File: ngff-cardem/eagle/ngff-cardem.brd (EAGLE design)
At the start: 90 x 100 mm, 146 parts, among them IC1 FPF2109, IC2 FPF2109, IC201 CB3Q3244PW, IC202 CB3Q3244PW, IC203 IP4234CZ6, IC302 TPS22958-DGN, J301 PJ-002BH-SMT-TR, M2 MENTOR_12701001, M3 MENTOR_12701001, Q201 12MHz, T1 BC847, T101 BC847, U201 IP4234CZ6, U202 AT91SAM3S-AU, U301 MIC5366-1.8YC5, X1 PINHD-2X3-SP, X102 ZX360D-B-10P(30), X201 MINI-USB-SHIELD-UX60-MB-5ST, X202 2.54mm, X3 JACK2.5_SJ-2523

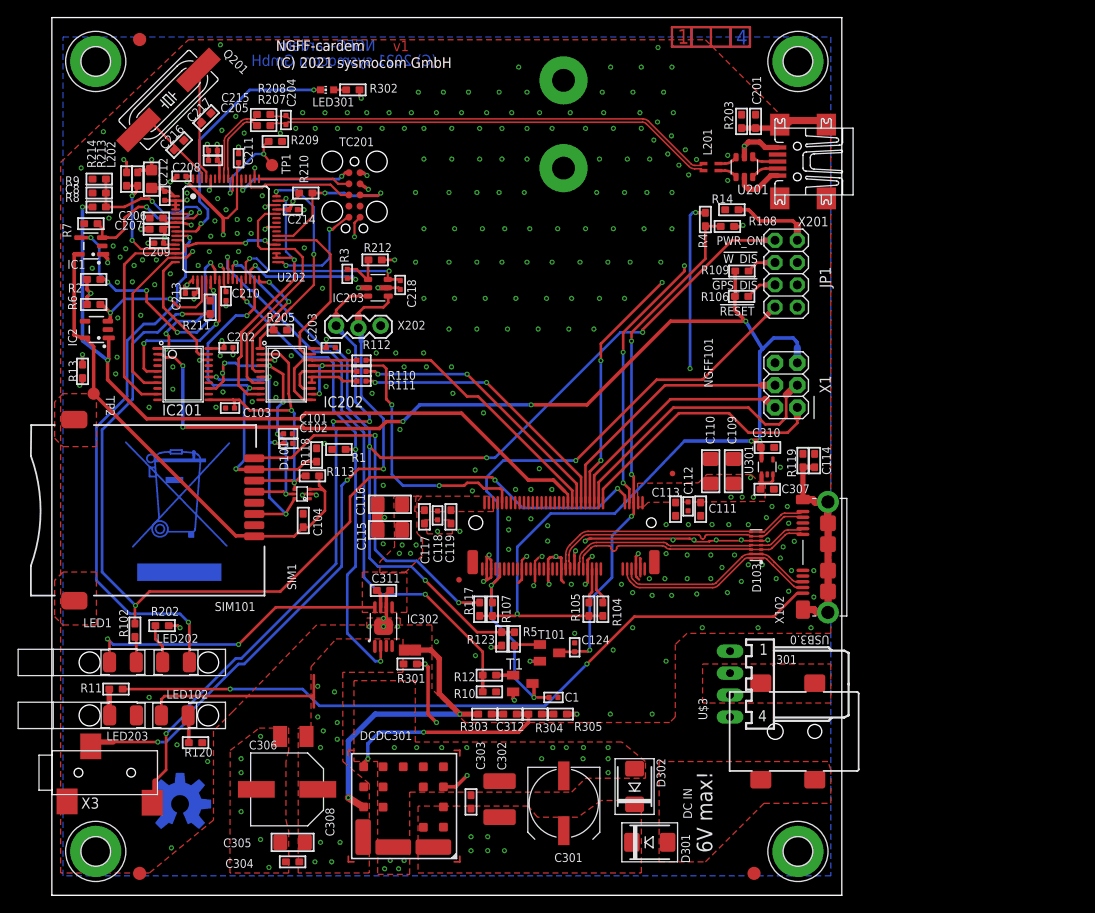
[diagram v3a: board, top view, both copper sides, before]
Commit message: ngff-cardem: add proper floppy power conn w/ a 2-resistor solder switch
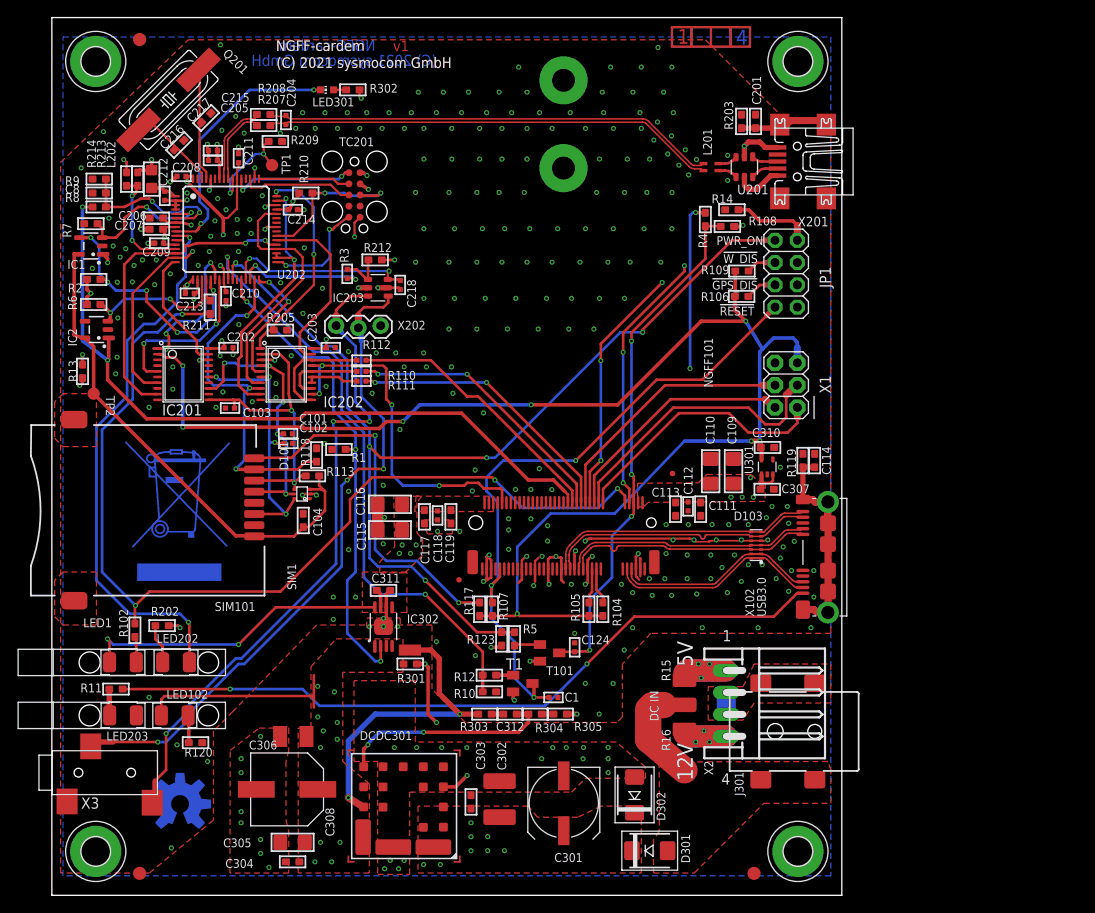
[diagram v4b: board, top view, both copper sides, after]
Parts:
- removed U$3: 171826-4-RA, 171826-4:171826-4
- added R15, R16: 0R, rc-sysmocom:1210
- added X2: 171826-4-RA, 171826-4:171826-4
- C311: value 100n -> 1n
- moved D301 0.95 mm to (68.1, 5.08)
- moved D302 0.95 mm to (66.4, 11.4)
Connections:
- new net N$23: R16.1, X2.4
- new net N$24: R15.2, X2.1
- net +VIN: now also R15.1, R16.2; no longer U$3.4
- net GND: now also X2.2, X2.3; no longer U$3.2, U$3.3
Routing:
- net N$24: track 0.00 -> 13.4 mm, vias 0 -> 3
- net +VIN: track 0.00 -> 13.3 mm
- net N$23: track 0.00 -> 12.8 mm, vias 0 -> 3
- net GND: track 98.3 -> 100.8 mm, vias 303 -> 312
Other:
- board text added: "12V"
- board text added: "5V"
- board text removed: "6V max!"

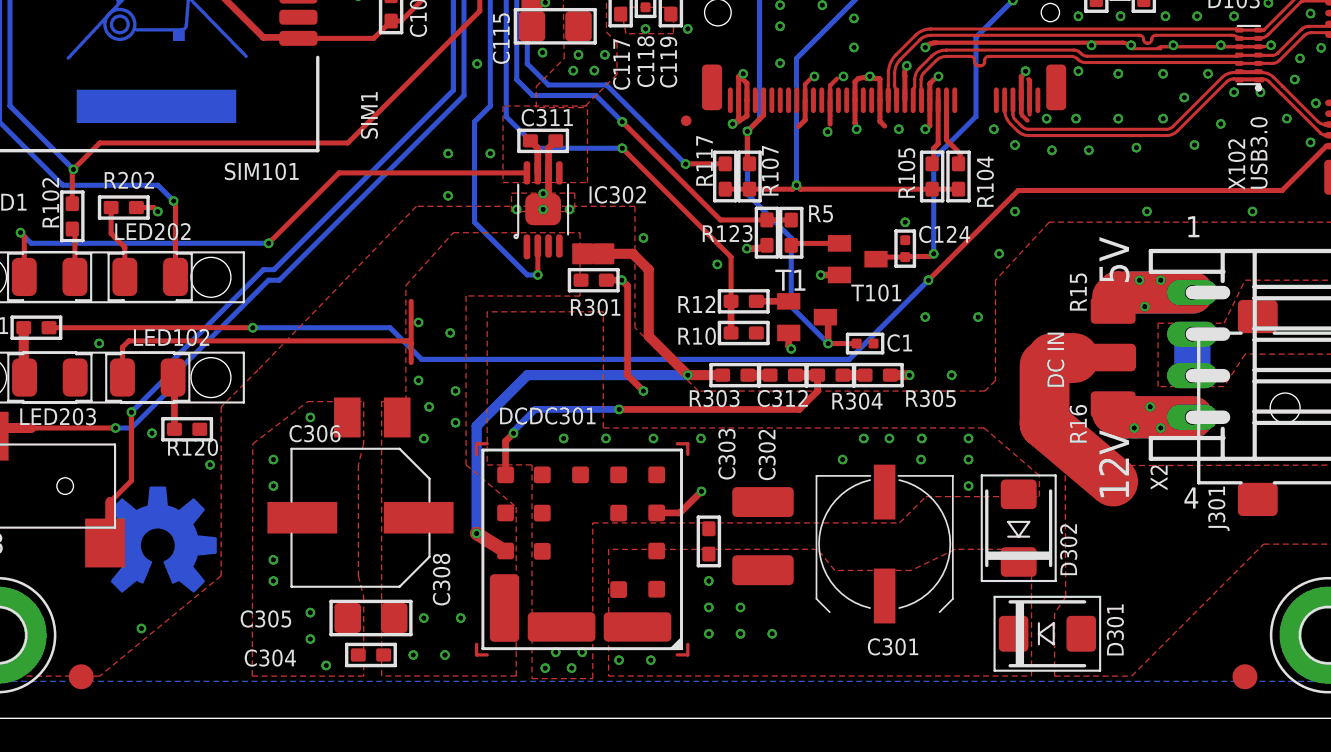
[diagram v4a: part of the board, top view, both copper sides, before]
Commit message: ngff-cardem: added a 2nd TPS22958 in VSSOP in parall due to availability
Now all four variant could be placed.
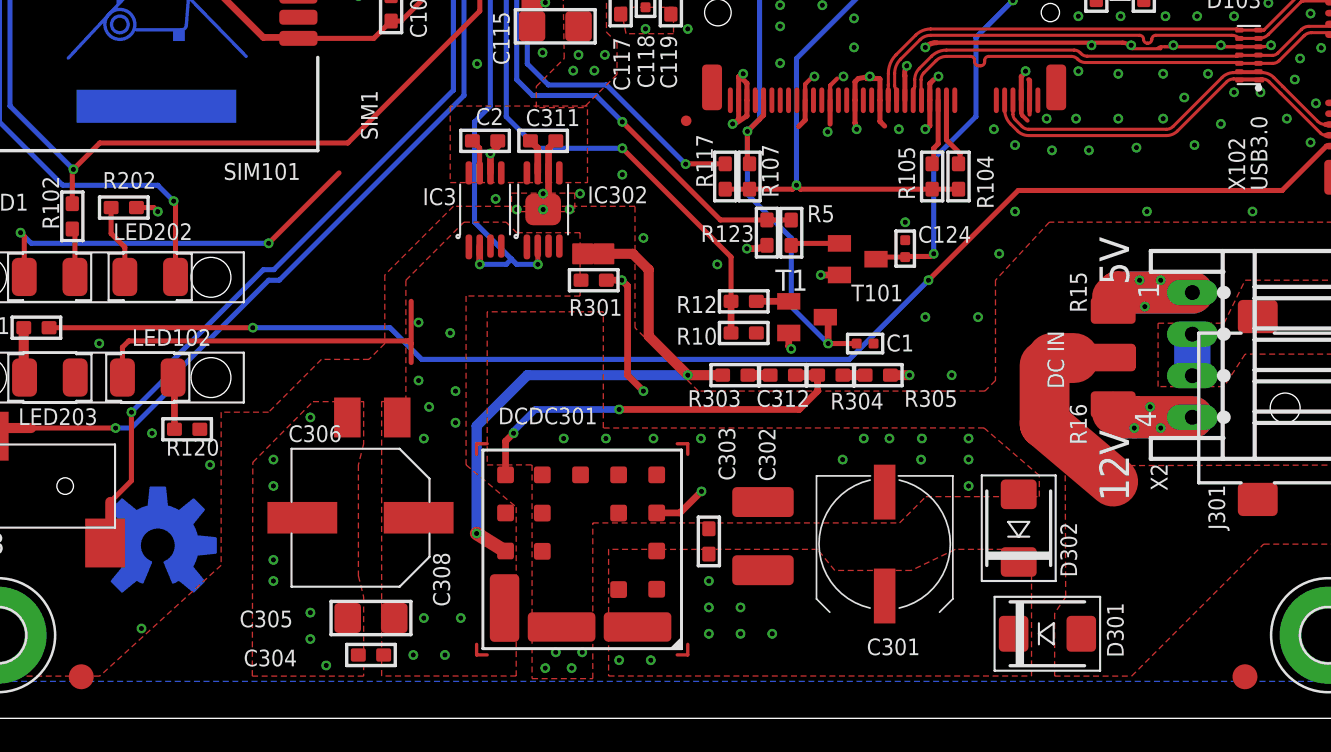
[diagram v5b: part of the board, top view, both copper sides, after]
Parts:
- added C2: 1n, rc-sysmocom:_0603
- added IC3: TPS22958N-DGK, TPS22958:VSSOP8
- IC302: value TPS22958-DGN -> TPS22958N-DGN; device TPS22958:VSSOP8-POWERPAD -> TPS22958:HVSSOP8
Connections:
- new net N$20: C2.2, IC3.7
- net GND: now also C2.1, IC3.6
- net MODEM_EN: now also IC3.2
- net VCC_3V3: now also IC3.1, IC3.3, IC3.4
- net V_MODEM: now also IC3.5, IC3.8
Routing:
- net V_MODEM: track 119.9 -> 108.6 mm
- net MODEM_EN: track 55.8 -> 58.0 mm, vias 3 -> 4
- net GND: track 100.8 -> 102.9 mm, vias 312 -> 313
- net N$20: track 0.00 -> 2.11 mm

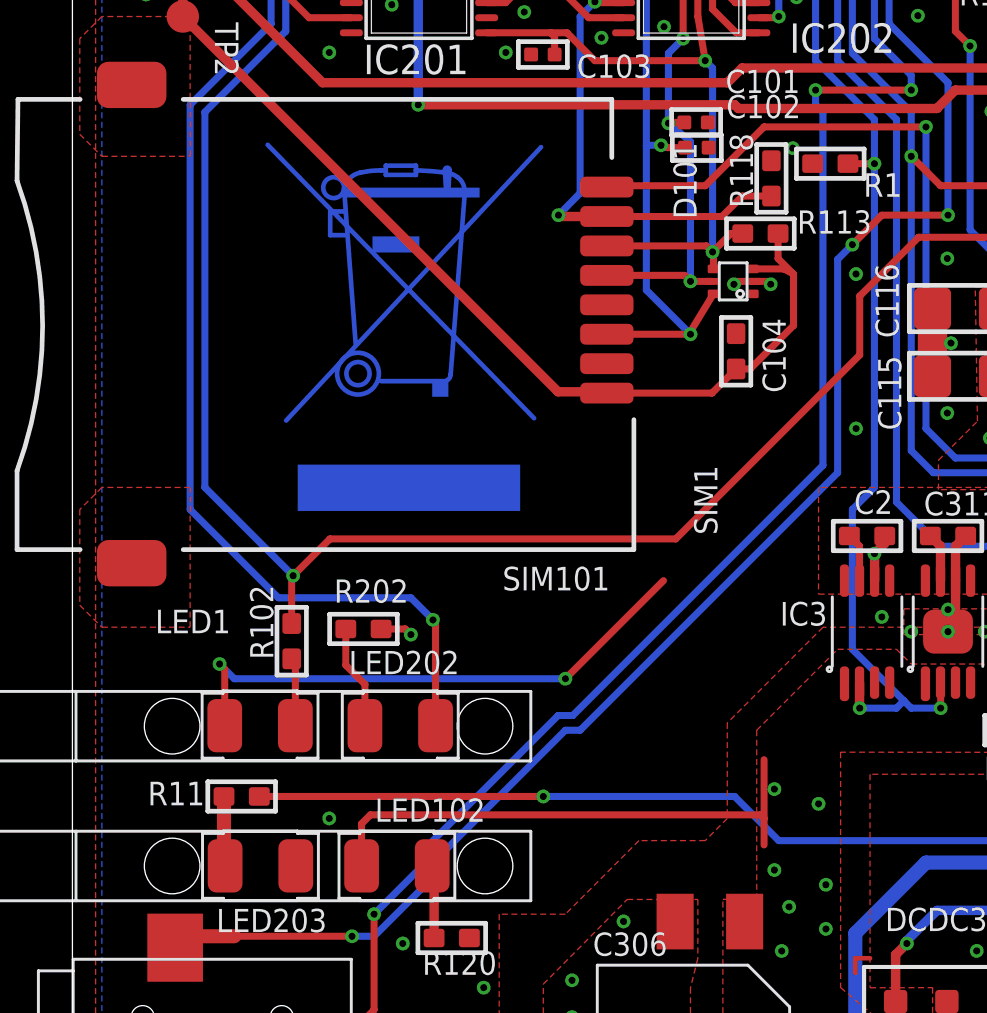
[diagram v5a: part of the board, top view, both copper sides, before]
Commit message: ngff-cardem: examine ERC + DRC for new part
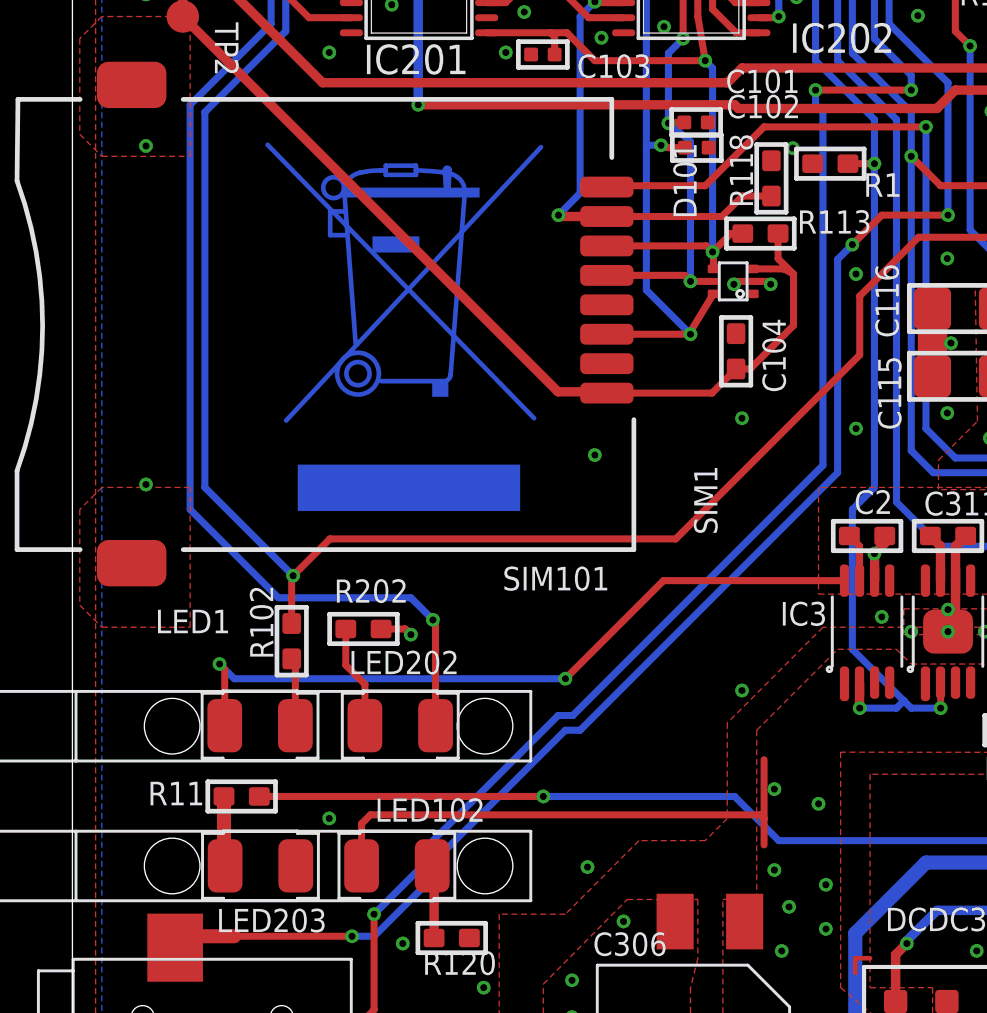
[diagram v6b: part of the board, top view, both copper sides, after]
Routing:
- net V_MODEM: track 108.6 -> 116.5 mm
- net GND: vias 313 -> 319
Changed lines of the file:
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@@
 <layers>
 <layer number="1" name="Top" color="4" fill="1" visible="yes" active="yes"/>
-<layer number="2" name="Route2" color="3" fill="3" visible="no" active="yes"/>
+<layer number="2" name="Route2" color="3" fill="3" visible="yes" active="yes"/>
 <layer number="3" name="Route3" color="4" fill="3" visible="no" active="no"/>
 <layer number="4" name="Route4" color="1" fill="4" visible="no" active="no"/>
@@
 <layer number="13" name="Route13" color="4" fill="5" visible="no" active="no"/>
 <layer number="14" name="Route14" color="1" fill="6" visible="no" active="no"/>
-<layer number="15" name="Route15" color="14" fill="6" visible="no" active="yes"/>
-<layer number="16" name="Bottom" color="1" fill="1" visible="no" active="yes"/>
+<layer number="15" name="Route15" color="14" fill="6" visible="yes" active="yes"/>
+<layer number="16" name="Bottom" color="1" fill="1" visible="yes" active="yes"/>
 <layer number="17" name="Pads" color="2" fill="1" visible="yes" active="yes"/>
 <layer number="18" name="Vias" color="2" fill="1" visible="yes" active="yes"/>
@@
 <via x="40.005" y="31.56" extent="1-16" drill="0.3"/>
 <via x="34.925" y="31.2425" extent="1-16" drill="0.3"/>
+<via x="22.5425" y="38.2275" extent="1-16" drill="0.3"/>
+<via x="3.175" y="36.9575" extent="1-16" drill="0.3"/>
+<via x="3.175" y="51.5625" extent="1-16" drill="0.3"/>
+<via x="28.8925" y="39.815" extent="1-16" drill="0.3"/>
+<via x="22.225" y="20.4475" extent="1-16" drill="0.3"/>
+<via x="28.8925" y="28.0675" extent="1-16" drill="0.3"/>
 </signal>
 <signal name="MDM_UIM_CLK">
@@
 <contactref element="IC3" pad="5"/>
 <contactref element="IC3" pad="8"/>
-<wire x1="33.315" y1="32.8075" x2="25.505" y2="32.8075" width="0" layer="19" extent="1-1"/>
+<wire x1="25.505" y1="32.8075" x2="33.315" y2="32.8075" width="0.3048" layer="1"/>
 </signal>
 <signal name="!NGFF_RESET">
